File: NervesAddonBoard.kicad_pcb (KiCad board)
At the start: 2 copper layers, 65 x 19 mm, 8 parts, among them J1 Conn_02x20_Odd_Even, J2 Conn_02x05_Odd_Even, J3 Grove_4pin_connector, J4 Grove_4pin_connector, J5 Grove_4pin_connector, J6 Grove_4pin_connector

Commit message: add silk
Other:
- board text added: "Nerves-Addon"
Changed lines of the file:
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@@
   (general
     (thickness 1.6)
-    (drawings 28)
+    (drawings 29)
     (tracks 95)
     (zones 0)
@@
   )
   (setup
-    (last_trace_width 0.2)
+    (last_trace_width 0.25)
     (user_trace_width 0.2)
     (trace_clearance 0.2)
@@
     )
   )
+  (gr_text Nerves-Addon (at 26.9 21.1) (layer F.SilkS)
+    (effects (font (size 1.2 1.2) (thickness 0.15)))
+  )
   (dimension 4.24 (width 0.15) (layer F.Fab)

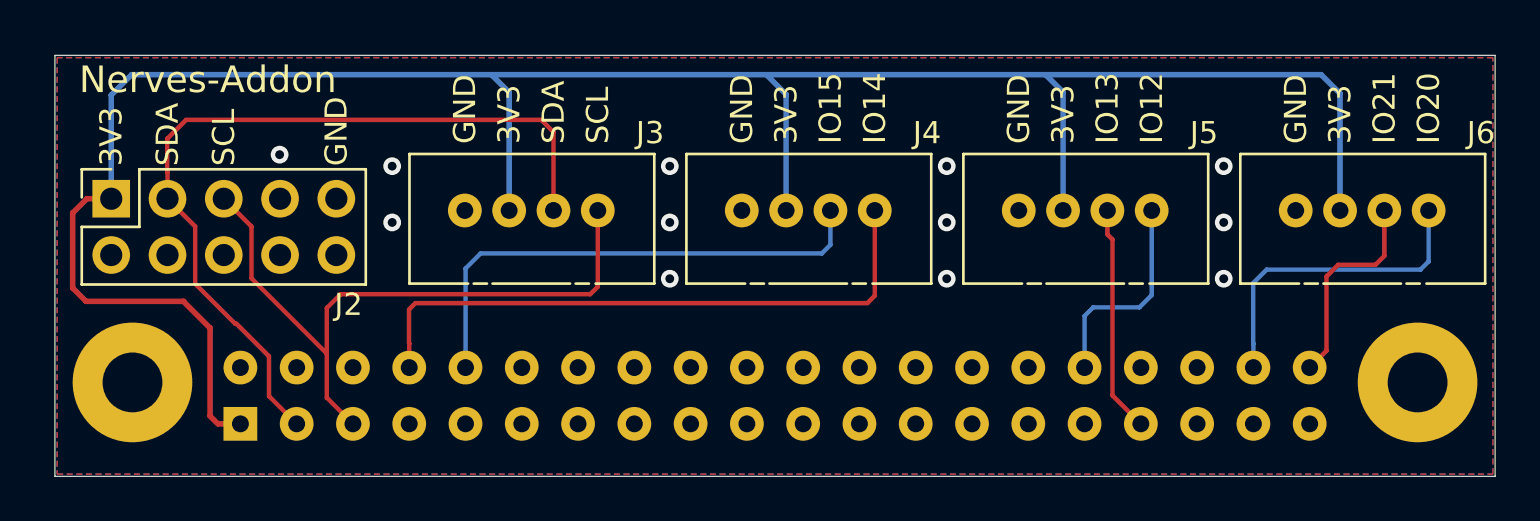
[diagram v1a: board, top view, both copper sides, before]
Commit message: change connector footprint
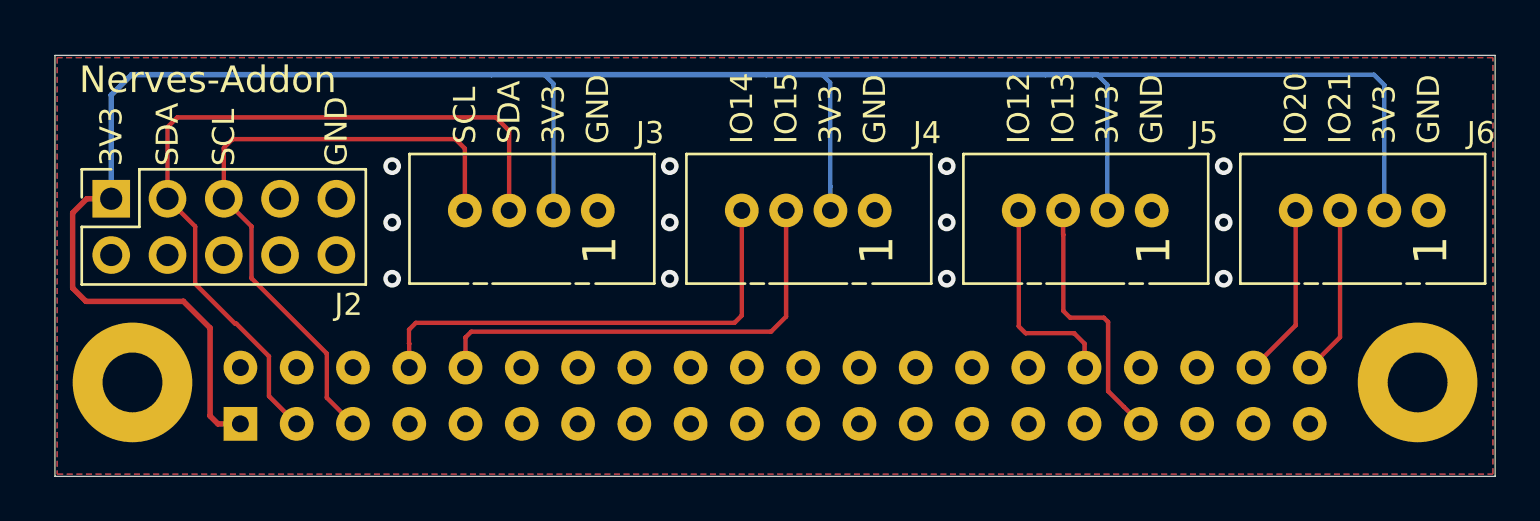
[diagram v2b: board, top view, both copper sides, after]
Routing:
- net /IO20: track 14.4 -> 7.88 mm
- net /IO14_TxD: track 27.8 -> 21.7 mm
- net /IO15_RxD: track 22.9 -> 21.0 mm
- net +3V3: track 104.5 -> 106.4 mm
- net /SCL: track 30.7 -> 28.9 mm
- net /IO21: track 9.47 -> 7.66 mm
- net /IO13_PWM1: track 10.3 -> 12.0 mm
- net /SDA: track 36.9 -> 35.3 mm
- net GND: vias 12 -> 11
- net (no net): vias 0 -> 1
